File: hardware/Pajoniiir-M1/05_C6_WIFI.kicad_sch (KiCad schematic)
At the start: 22 parts, among them U4 ESP32-C6-WROOM-1-N4

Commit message: hardware: normalize schematic reference designators
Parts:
- renumbered C_C6_HF to C64, C_C6_LOCAL to C65, C_C6_BULK to C66, C_C6_EN to C67, R_C6_RESET_SER to R42, R_C6_EN to R43, R_SDIO_CMD to R44, R_SDIO_CMD_PU to R45, R_SDIO_CLK to R46, R_SDIO_D0 to R47, R_SDIO_D0_PU to R48, R_SDIO_D1 to R49, R_SDIO_D1_PU to R50, R_SDIO_D2 to R51, R_SDIO_D2_PU to R52, R_SDIO_D3 to R53, R_SDIO_D3_PU to R54, R_C6_UART_TX to R55, R_C6_UART_RX to R56, R_C6_GPIO8_PU to R57, R_C6_GPIO9_PU to R58
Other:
- note added: "3V3_C6 isolation/tuning link is implemented once in 02_POWER_3V3 (FB1). Do not duplicate it here."
- note removed: "3V3_C6 isolation/tuning link is implemented once in 02_POWER_3V3 (FB_C6). Do not duplicate it here."

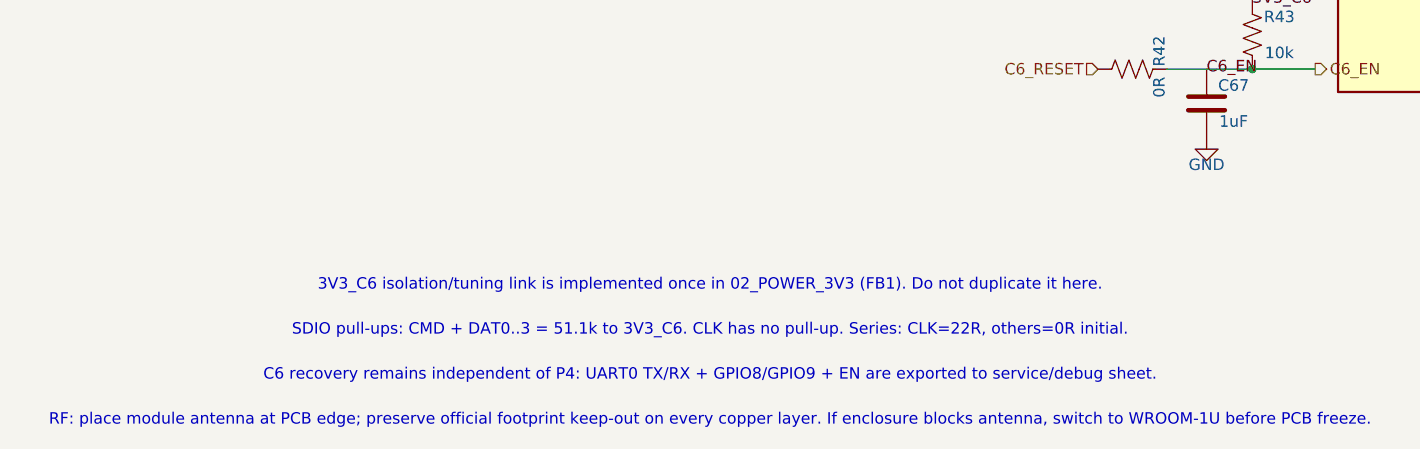
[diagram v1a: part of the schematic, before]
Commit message: hardware: constrain RefDes migration to annotation fields
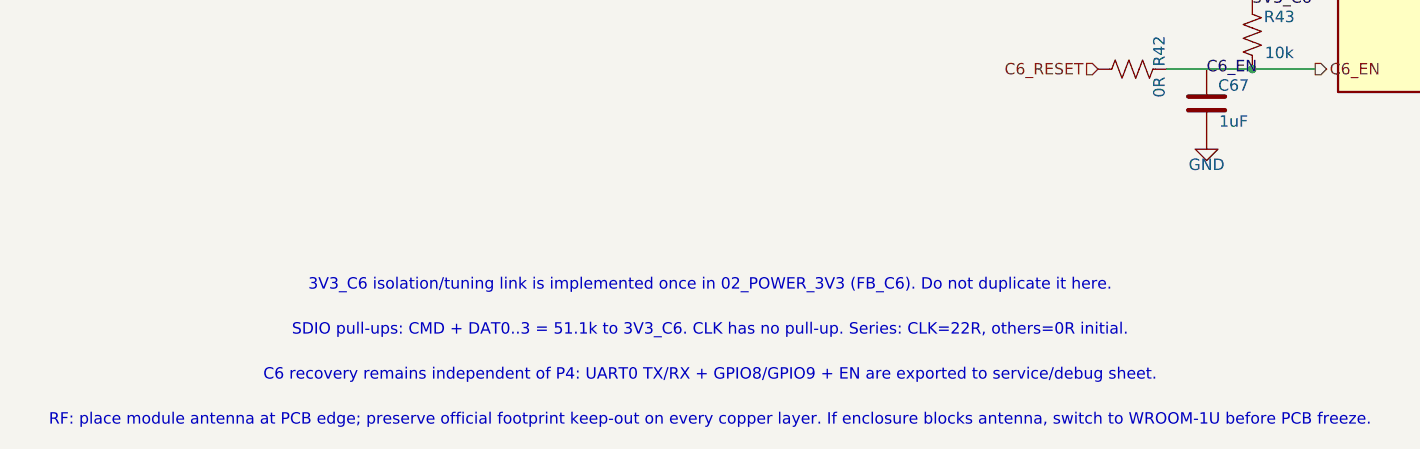
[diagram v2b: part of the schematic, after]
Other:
- note added: "3V3_C6 isolation/tuning link is implemented once in 02_POWER_3V3 (FB_C6). Do not duplicate it here."
- note removed: "3V3_C6 isolation/tuning link is implemented once in 02_POWER_3V3 (FB1). Do not duplicate it here."
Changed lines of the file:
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@@
   (no_connect (at 158.115 80.01))
   (no_connect (at 158.115 82.55))
-  (text "3V3_C6 isolation/tuning link is implemented once in 02_POWER_3V3 (FB1). Do not duplicate it here." (exclude_from_sim no) (at 35 132 0) (effects (font (size 1.27 1.27))))
+  (text "3V3_C6 isolation/tuning link is implemented once in 02_POWER_3V3 (FB_C6). Do not duplicate it here." (exclude_from_sim no) (at 35 132 0) (effects (font (size 1.27 1.27))))
   (text "SDIO pull-ups: CMD + DAT0..3 = 51.1k to 3V3_C6. CLK has no pull-up. Series: CLK=22R, others=0R initial." (exclude_from_sim no) (at 35 137 0) (effects (font (size 1.27 1.27))))
   (text "C6 recovery remains independent of P4: UART0 TX/RX + GPIO8/GPIO9 + EN are exported to service/debug sheet." (exclude_from_sim no) (at 35 142 0) (effects (font (size 1.27 1.27))))
